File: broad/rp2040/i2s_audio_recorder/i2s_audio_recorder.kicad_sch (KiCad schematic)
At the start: 55 parts, among them J1 USB_C_Receptacle_USB2.0_16P, J2 Conn_01x04_Pin, J3 SD_Card_Device, J4 Conn_01x08_Pin, J5 Conn_01x08_Pin, J6 Conn_01x08_Pin, SW1 TS-1101-C-W, SW2 TS-1101-C-W, SW3 TS-1101-C-W, SW4 TS-1101-C-W, U1 MSM261S4030H0R, U1 SMBJ5.0CA, U2 RP2040, U3 SMBJ5.0CA, U4 SMBJ5.0CA, U5 AMS1117-3.3, U7 W25Q128JVS, Y1 12M

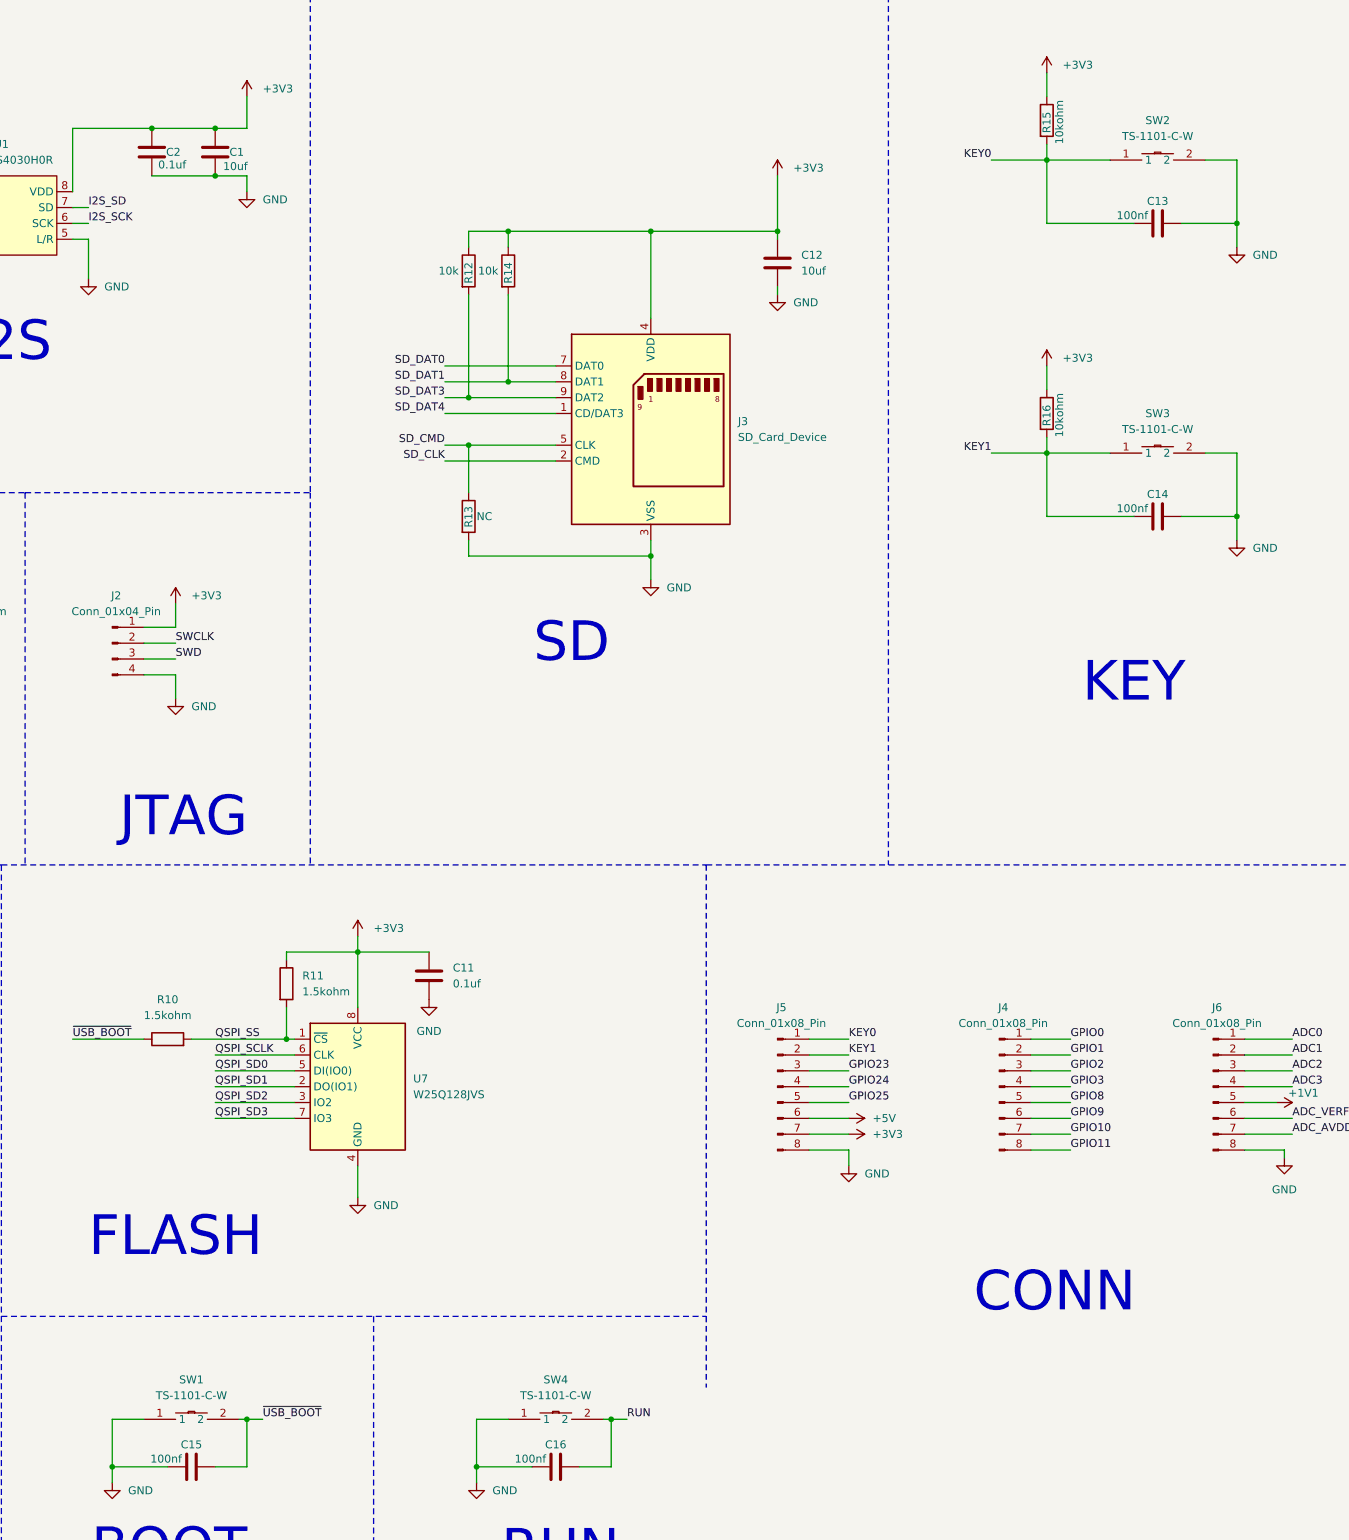
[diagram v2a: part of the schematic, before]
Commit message: Update footprint of SD card in `i2s_audio_recorder`
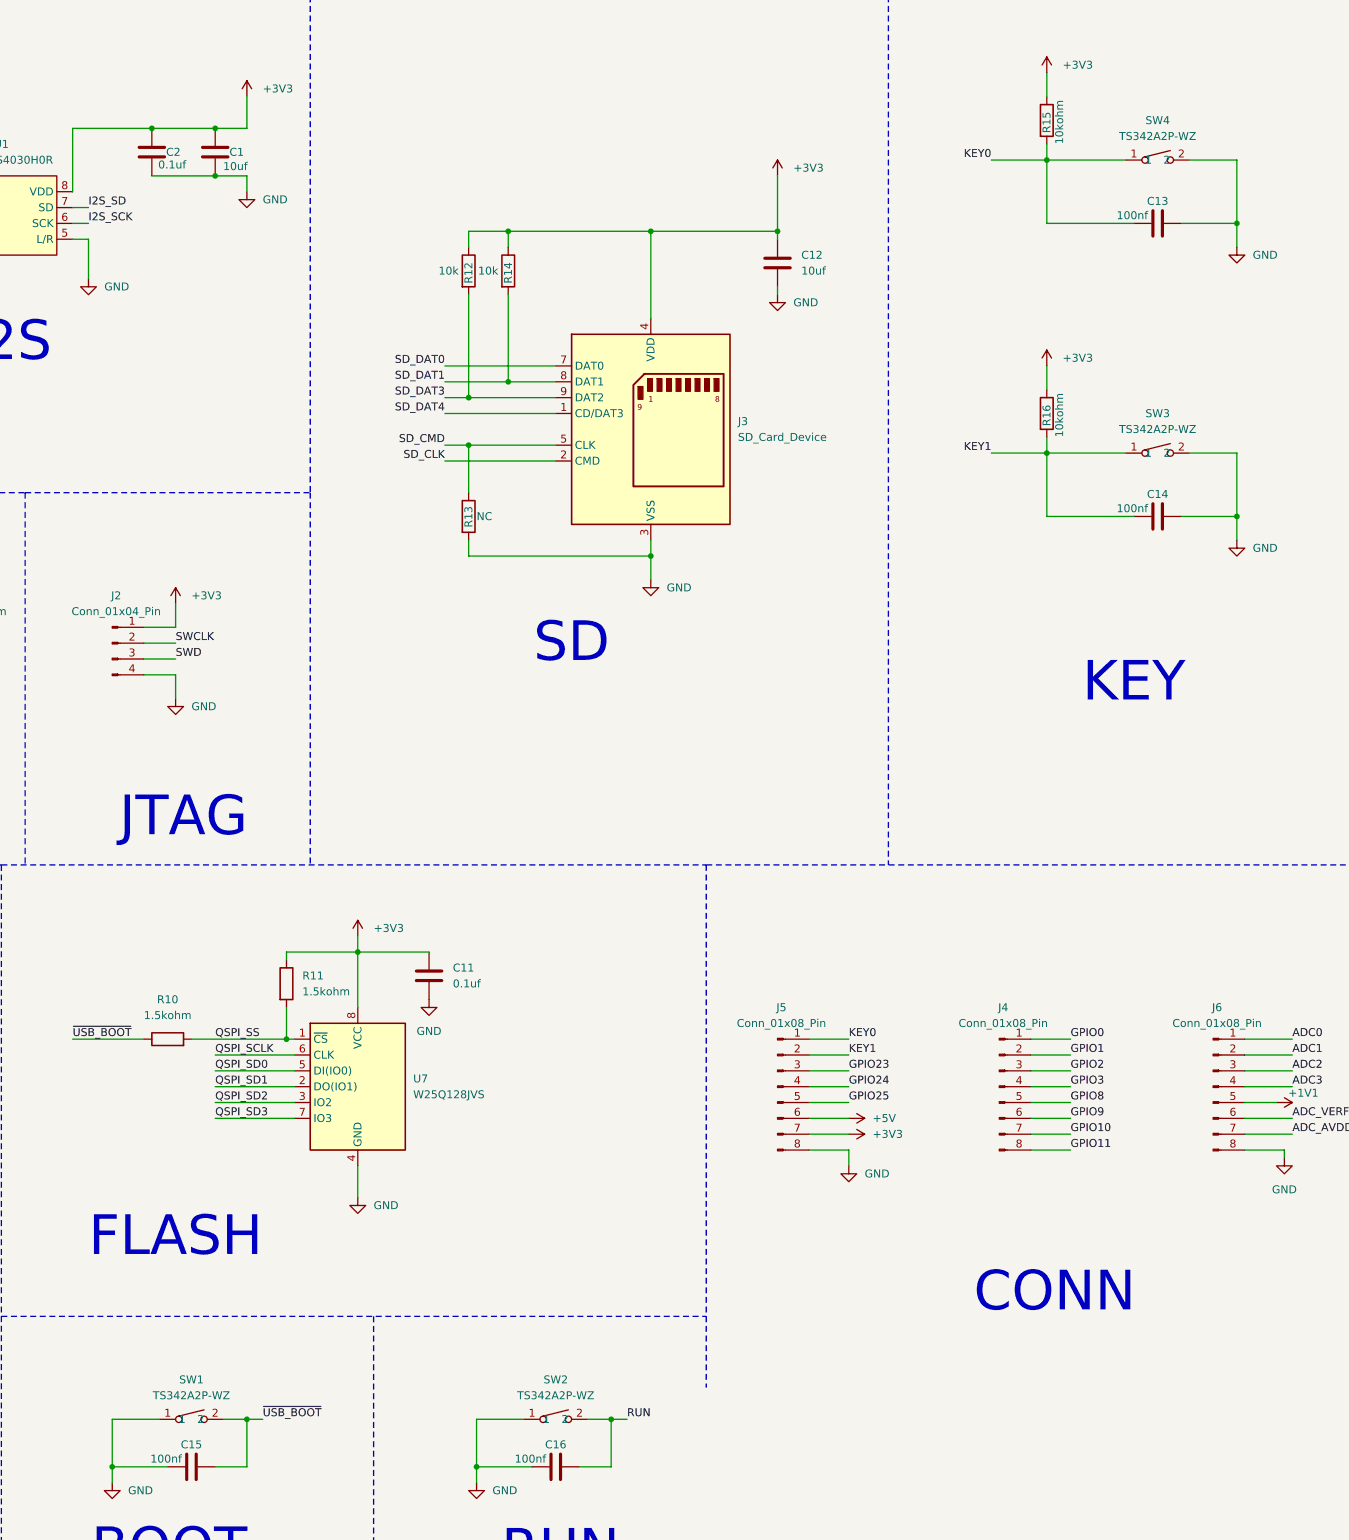
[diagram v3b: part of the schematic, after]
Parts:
- removed SW1, SW2, SW3, SW4: TS-1101-C-W, easyeda2kicad:SW-SMD_L6.0-W3.3-LS8.0, symbol easyeda2kicad:TS-1101-C-W
- added SW1, SW2, SW3, SW4: TS342A2P-WZ, easyeda2kicad:SW-SMD_L4.0-W2.9-LS5.0, symbol easyeda2kicad:TS342A2P-WZ
- J3: footprint Connector_Card:microSD_HC_Hirose_DM3AT-SF-PEJM5 -> easyeda2kicad:TF-SMD_TF-123-ARP9H15
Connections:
- net GND: now also SW1.1, SW2.1, SW3.2, SW4.2
- net KEY0: now also SW4.1
- net KEY1: now also SW3.1
- net RUN: now also SW2.2
- net ~{USB_BOOT}: now also SW1.2
